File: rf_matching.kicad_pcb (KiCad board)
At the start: 2 copper layers, 46.6 x 32.6 mm, 12 parts, among them J1 RFI, J2 RFO, J3 CTRL, J4 ANT, J5 3V3, U1 pe4259ds, U2 SF2098

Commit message: Add thicker bias, add PCB LOSS line
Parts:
- added J6: PCB_LOSS_IN, KiCad/Connectors_Molex.pretty:Molex_SMA_Jack_Edge_Mount, F.Cu at (160.0, 117.0)
- added J7: PCB_LOSS_OUT, KiCad/Connectors_Molex.pretty:Molex_SMA_Jack_Edge_Mount, F.Cu at (194.1, 117.0)
- moved J5 23.7 mm to (193.7, 70.3), turned to 180 degrees
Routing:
- net GND: track 46.8 -> 6.83 mm
- net Net-(J6-Pad1): track 0.00 -> 37.5 mm
- net Net-(J5-Pad1): track 5.26 -> 35.6 mm
- net Net-(C2-Pad2): track 10.4 -> 9.69 mm
- net Net-(C3-Pad2): track 10.4 -> 9.79 mm
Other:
- board size 46.6 x 32.6 mm -> 46.8 x 63.1 mm

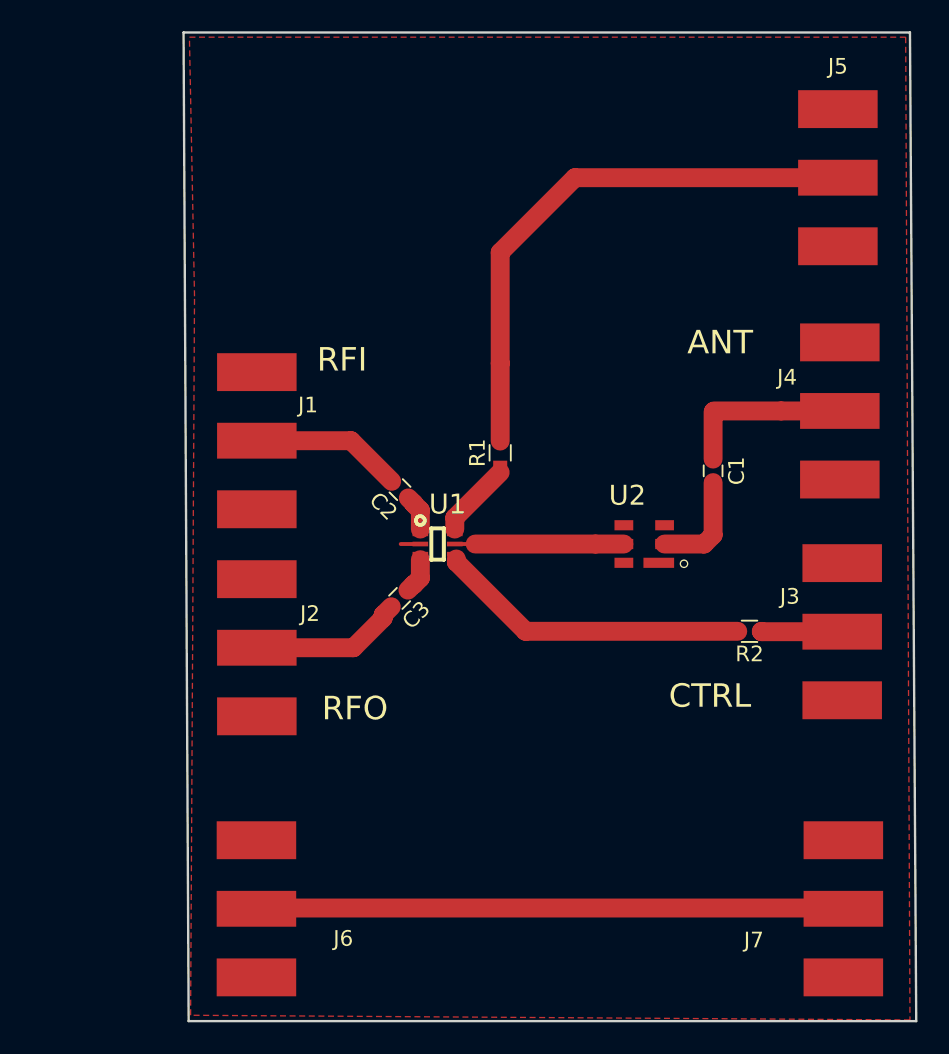
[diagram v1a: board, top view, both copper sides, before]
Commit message: Redesign, more similar to official evaluation board
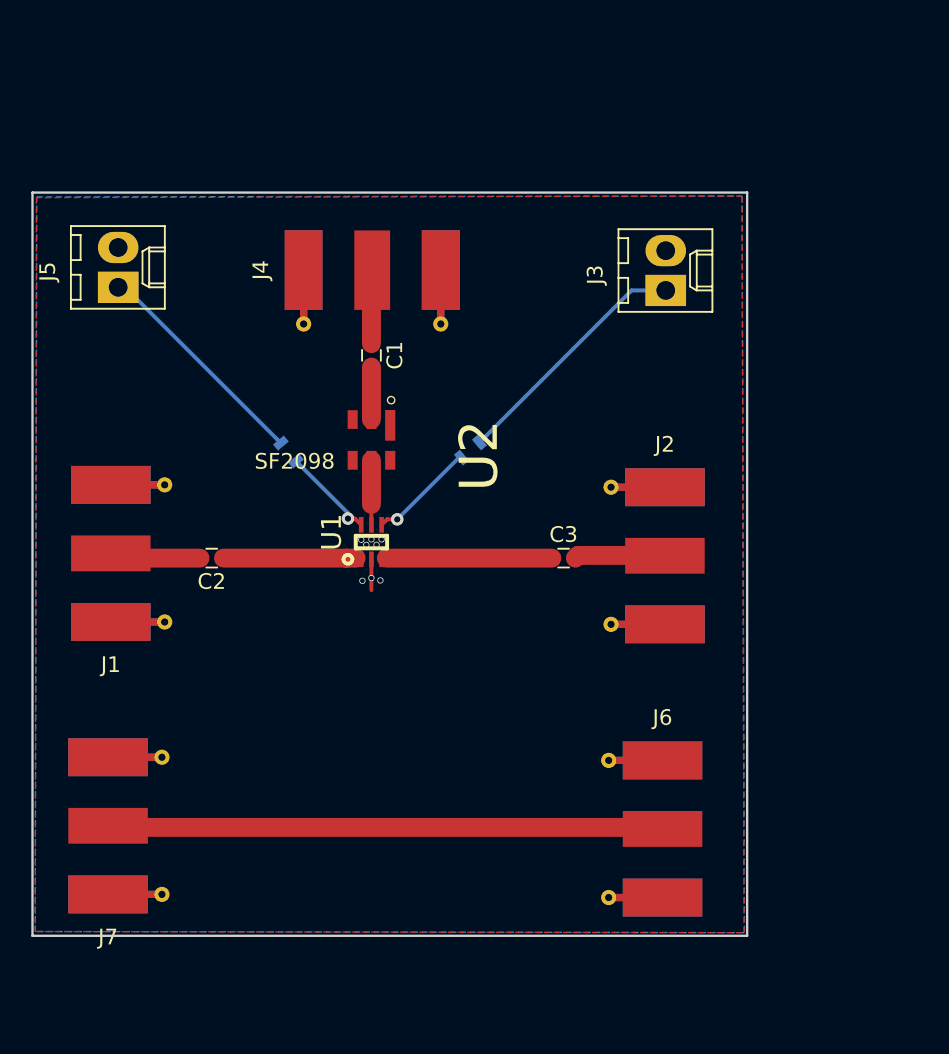
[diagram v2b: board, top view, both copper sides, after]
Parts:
- J3: footprint KiCad/Connectors_Molex.pretty:Molex_SMA_Jack_Edge_Mount -> KiCad/Connectors_Molex.pretty:Molex_KK-6410-02_02x2.54mm_Straight
- J5: value 3V3 -> VDD; footprint KiCad/Connectors_Molex.pretty:Molex_SMA_Jack_Edge_Mount -> KiCad/Connectors_Molex.pretty:Molex_KK-6410-02_02x2.54mm_Straight
- R1, R2: moved to B.Cu
- moved J5 44.8 mm to (149.5, 77.3), turned to 90 degrees
- moved J7 43.8 mm to (150.6, 111.8), turned to 0 degrees
- moved J4 29.1 mm to (165.7, 78.0), turned to 270 degrees
- moved J3 23.8 mm to (184.4, 77.5), turned to 90 degrees
- moved J2 23.4 mm to (182.7, 94.5), turned to 180 degrees
- moved J6 23.1 mm to (182.5, 112.0), turned to 180 degrees
- moved C1 23.0 mm to (165.7, 81.7)
- moved R2 21.3 mm to (172.0, 87.8), turned to 220 degrees
- moved U2 18.7 mm to (165.7, 87.1), turned to 270 degrees
- moved R1 13.5 mm to (160.3, 87.9), turned to 130 degrees
- moved C2 12.8 mm to (155.4, 94.7), turned to 180 degrees
- moved J1 11.8 mm to (150.7, 94.3)
- moved C3 10.8 mm to (177.9, 94.7), turned to 0 degrees
- moved U1 4.23 mm to (165.7, 93.6), turned to 270 degrees
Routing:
- net GND: track 6.83 -> 36.4 mm, vias 0 -> 8
- net Net-(J5-Pad1): track 35.6 -> 14.5 mm
- net Net-(R2-Pad2): track 20.5 -> 6.88 mm, vias 0 -> 1
- net Net-(J3-Pad1): track 5.18 -> 16.2 mm
- net Net-(C3-Pad1): track 2.64 -> 10.9 mm
- net Net-(U1-Pad5): track 10.8 -> 4.12 mm
- net Net-(C2-Pad1): track 2.61 -> 8.83 mm
- net Net-(C1-Pad1): track 11.1 -> 5.72 mm
- net Net-(C2-Pad2): track 9.69 -> 6.04 mm
- net Net-(C3-Pad2): track 9.79 -> 6.37 mm
- net Net-(C1-Pad2): track 6.69 -> 3.35 mm
- net Net-(J6-Pad1): track 37.5 -> 36.2 mm
- net Net-(R1-Pad1): track 5.63 -> 6.07 mm, vias 0 -> 1
- added copper zone on B.Cu, net GND
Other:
- board size 46.8 x 63.1 mm -> 45.7 x 47.5 mm
- board text removed: "ANT"
- board text removed: "CTRL"
- board text removed: "RFI"
- board text removed: "RFO"

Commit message: Add by-hand vias, silly semi-random placement
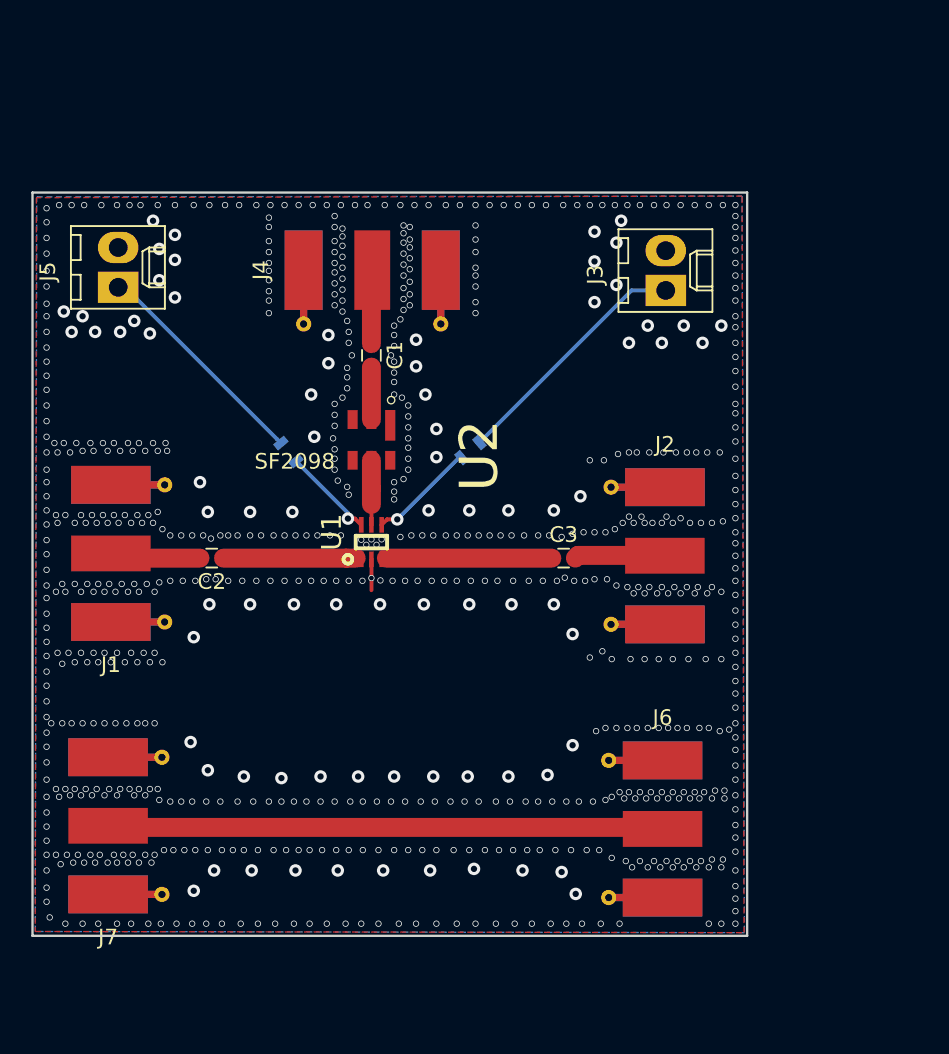
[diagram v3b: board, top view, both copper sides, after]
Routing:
- net GND: vias 8 -> 726
- net (no net): vias 0 -> 2

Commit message: Add current iteration image, boards sent to Seed Studios via promotion pricing: https://twitter.com/braincode/status/1036909730244034560
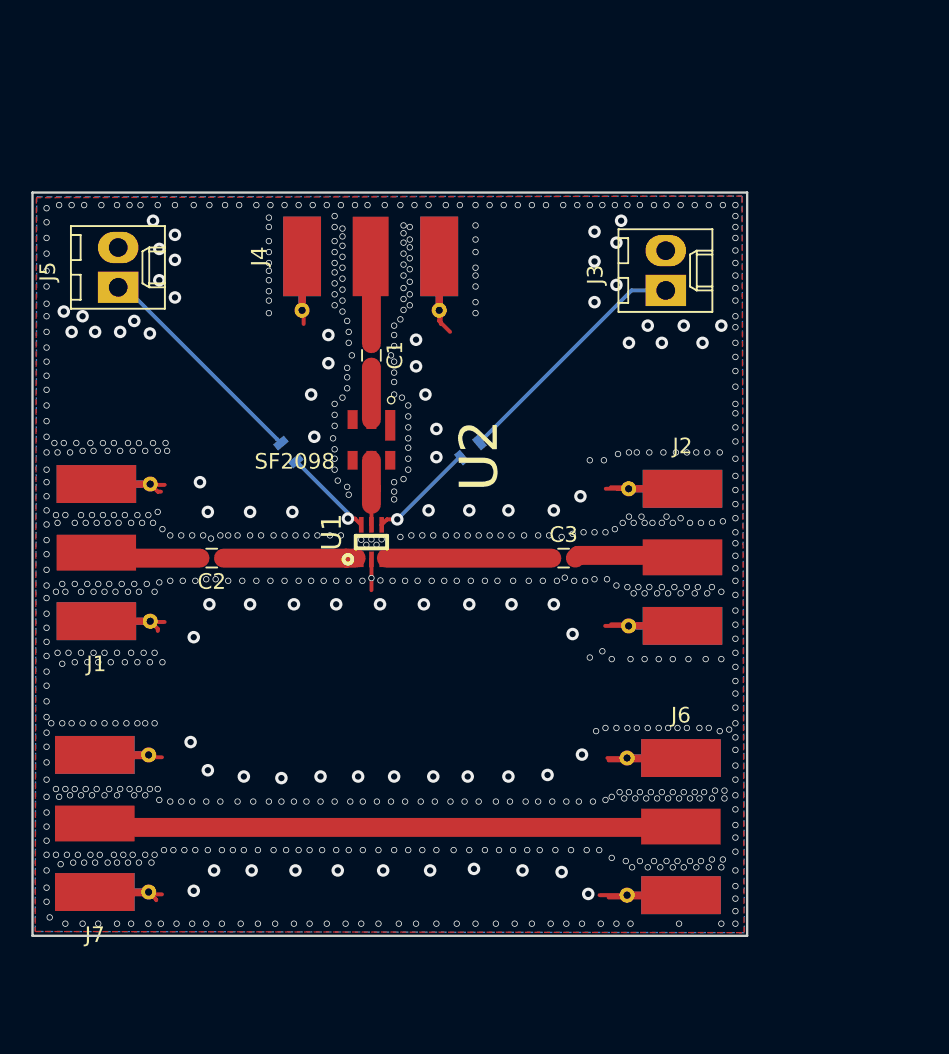
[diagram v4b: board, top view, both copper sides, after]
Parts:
- moved J6 1.18 mm to (183.7, 111.8)
- moved J2 1.13 mm to (183.8, 94.6)
- moved J1 0.93 mm to (149.8, 94.3)
- moved J4 0.88 mm to (165.6, 77.1)
- moved J7 0.86 mm to (149.7, 111.6)
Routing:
- net GND: track 36.4 -> 47.2 mm, vias 726 -> 729
- net (no net): vias 2 -> 0
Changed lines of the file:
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@@
   (thickness 1.6)
   (drawings 7)
-  (tracks 773)
+  (tracks 788)
   (zones 0)
   (modules 14)
@@
   (thickness 1.6)
   (drawings 7)
-  (tracks 773)
+  (tracks 788)
   (zones 0)
   (modules 14)
@@
   (visible_elements FFFFFFFF)
   (pcbplotparams
-    (layerselection 0x00020_7fffffff)
-    (usegerberextensions false)
+    (layerselection 0x010f0_ffffffff)
+    (usegerberextensions true)
     (usegerberattributes true)
     (usegerberadvancedattributes true)
@@
     (viasonmask false)
     (mode 1)
-    (useauxorigin true)
+    (useauxorigin false)
     (hpglpennumber 1)
     (hpglpenspeed 20)
@@
   )
   (module KiCad/Connectors_Molex.pretty:Molex_SMA_Jack_Edge_Mount (layer F.Cu)
-    (at 150.725 94.35)
+    (at 149.8 94.3)
     (descr "Molex SMA Jack, Edge Mount, http://www.molex.com/pdm_docs/sd/732511150_sd.pdf")
     (tags "sma edge")
@@
   )
   (module KiCad/Connectors_Molex.pretty:Molex_SMA_Jack_Edge_Mount (layer F.Cu)
-    (at 182.675 94.5 180)
+    (at 183.8 94.6 180)
     (descr "Molex SMA Jack, Edge Mount, http://www.molex.com/pdm_docs/sd/732511150_sd.pdf")
     (tags "sma edge")
@@
   )
   (module KiCad/Connectors_Molex.pretty:Molex_SMA_Jack_Edge_Mount (layer F.Cu)
-    (at 165.7 77.975 270)
+    (at 165.6 77.1 270)
     (descr "Molex SMA Jack, Edge Mount, http://www.molex.com/pdm_docs/sd/732511150_sd.pdf")
     (tags "sma edge")
@@
   )
   (module KiCad/Connectors_Molex.pretty:Molex_SMA_Jack_Edge_Mount (layer F.Cu)
-    (at 182.525 111.95 180)
+    (at 183.7 111.8 180)
     (descr "Molex SMA Jack, Edge Mount, http://www.molex.com/pdm_docs/sd/732511150_sd.pdf")
     (tags "sma edge")
@@
   )
   (module KiCad/Connectors_Molex.pretty:Molex_SMA_Jack_Edge_Mount (layer F.Cu)
-    (at 150.55 111.75)
+    (at 149.7 111.6)
     (descr "Molex SMA Jack, Edge Mount, http://www.molex.com/pdm_docs/sd/732511150_sd.pdf")
     (tags "sma edge")
@@
   (gr_line (start 189.65 118.775) (end 189.65 71.3) (layer Edge.Cuts) (width 0.15))
   (gr_line (start 144 118.775) (end 189.65 118.775) (layer Edge.Cuts) (width 0.15))
-  (via (at 187.2 118) (size 0.4) (drill 0.3) (layers F.Cu B.Cu) (net 0))
-  (via (at 181.5 118) (size 0.4) (drill 0.3) (layers F.Cu B.Cu) (net 0))
   (segment (start 165.65 85.8) (end 165.65 82.45) (width 1.20904) (layer F.Cu) (net 1))
   (segment (start 165.65 80.95) (end 165.65 75.23) (width 1.20904) (layer F.Cu) (net 2))
@@
   (segment (start 166.529521 94.725) (end 166.604521 94.65) (width 0.25) (layer F.Cu) (net 6))
   (segment (start 177.175 94.65) (end 166.604521 94.65) (width 1.20904) (layer F.Cu) (net 6))
+  (segment (start 169.98 78.82) (end 169.98 79.505893) (width 0.25) (layer F.Cu) (net 7))
+  (segment (start 169.98 79.505893) (end 170.674107 80.2) (width 0.25) (layer F.Cu) (net 7))
+  (segment (start 151.42 115.98) (end 151.904999 116.464999) (width 0.25) (layer F.Cu) (net 7))
+  (segment (start 151.904999 116.464999) (end 151.904999 116.504999) (width 0.25) (layer F.Cu) (net 7))
+  (segment (start 151.52 98.68) (end 152.004999 99.164999) (width 0.25) (layer F.Cu) (net 7))
+  (segment (start 152.004999 99.164999) (end 152.004999 99.304999) (width 0.25) (layer F.Cu) (net 7))
+  (segment (start 151.52 89.92) (end 152.004999 90.404999) (width 0.25) (layer F.Cu) (net 7))
+  (segment (start 152.004999 90.404999) (end 152.204999 90.404999) (width 0.25) (layer F.Cu) (net 7))
+  (via (at 185.3 118) (size 0.4) (drill 0.3) (layers F.Cu B.Cu) (net 7))
+  (via (at 182.2 118) (size 0.4) (drill 0.3) (layers F.Cu B.Cu) (net 7))
+  (via (at 181.3 118) (size 0.4) (drill 0.3) (layers F.Cu B.Cu) (net 7))
+  (segment (start 181.98 116.18) (end 180.22 116.18) (width 0.25) (layer F.Cu) (net 7))
+  (segment (start 181.98 107.42) (end 180.72 107.42) (width 0.25) (layer F.Cu) (net 7))
+  (segment (start 182.08 90.22) (end 180.62 90.22) (width 0.25) (layer F.Cu) (net 7))
+  (segment (start 182.08 90.22) (end 181.394107 90.22) (width 0.25) (layer F.Cu) (net 7))
+  (segment (start 181.394107 90.22) (end 181.374107 90.2) (width 0.25) (layer F.Cu) (net 7))
+  (segment (start 182.08 98.98) (end 180.58 98.98) (width 0.25) (layer F.Cu) (net 7))
   (via (at 149.9 91.9) (size 0.4) (drill 0.3) (layers F.Cu B.Cu) (net 7))
   (via (at 149.2 91.9) (size 0.4) (drill 0.3) (layers F.Cu B.Cu) (net 7))
@@
   (via (at 161.8 84.2) (size 0.8) (drill 0.4) (layers F.Cu B.Cu) (net 7))
   (via (at 162 86.9) (size 0.8) (drill 0.4) (layers F.Cu B.Cu) (net 7))
-  (via (at 178.7 116.1) (size 0.8) (drill 0.4) (layers F.Cu B.Cu) (net 7))
+  (via (at 179.5 116.1) (size 0.8) (drill 0.4) (layers F.Cu B.Cu) (net 7))
   (via (at 177.8 114.7) (size 0.8) (drill 0.4) (layers F.Cu B.Cu) (net 7))
   (via (at 175.3 114.6) (size 0.8) (drill 0.4) (layers F.Cu B.Cu) (net 7))
@@
   (via (at 155.6 114.6) (size 0.8) (drill 0.4) (layers F.Cu B.Cu) (net 7))
   (via (at 154.3 115.9) (size 0.8) (drill 0.4) (layers F.Cu B.Cu) (net 7))
-  (via (at 178.5 106.6) (size 0.8) (drill 0.4) (layers F.Cu B.Cu) (net 7))
+  (via (at 179.1 107.2) (size 0.8) (drill 0.4) (layers F.Cu B.Cu) (net 7))
   (via (at 176.9 108.5) (size 0.8) (drill 0.4) (layers F.Cu B.Cu) (net 7))
   (via (at 174.4 108.6) (size 0.8) (drill 0.4) (layers F.Cu B.Cu) (net 7))
